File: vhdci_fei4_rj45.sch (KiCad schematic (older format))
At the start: 43 parts, among them J1 71430-015, J2 RJ45, J3 RJ45, J4 RJ45, J5 RJ45, J6 RJ45, J7 RJ45, J8 RJ45, J9 RJ45, P1 USB_OTG, U1 LM317_SOT223

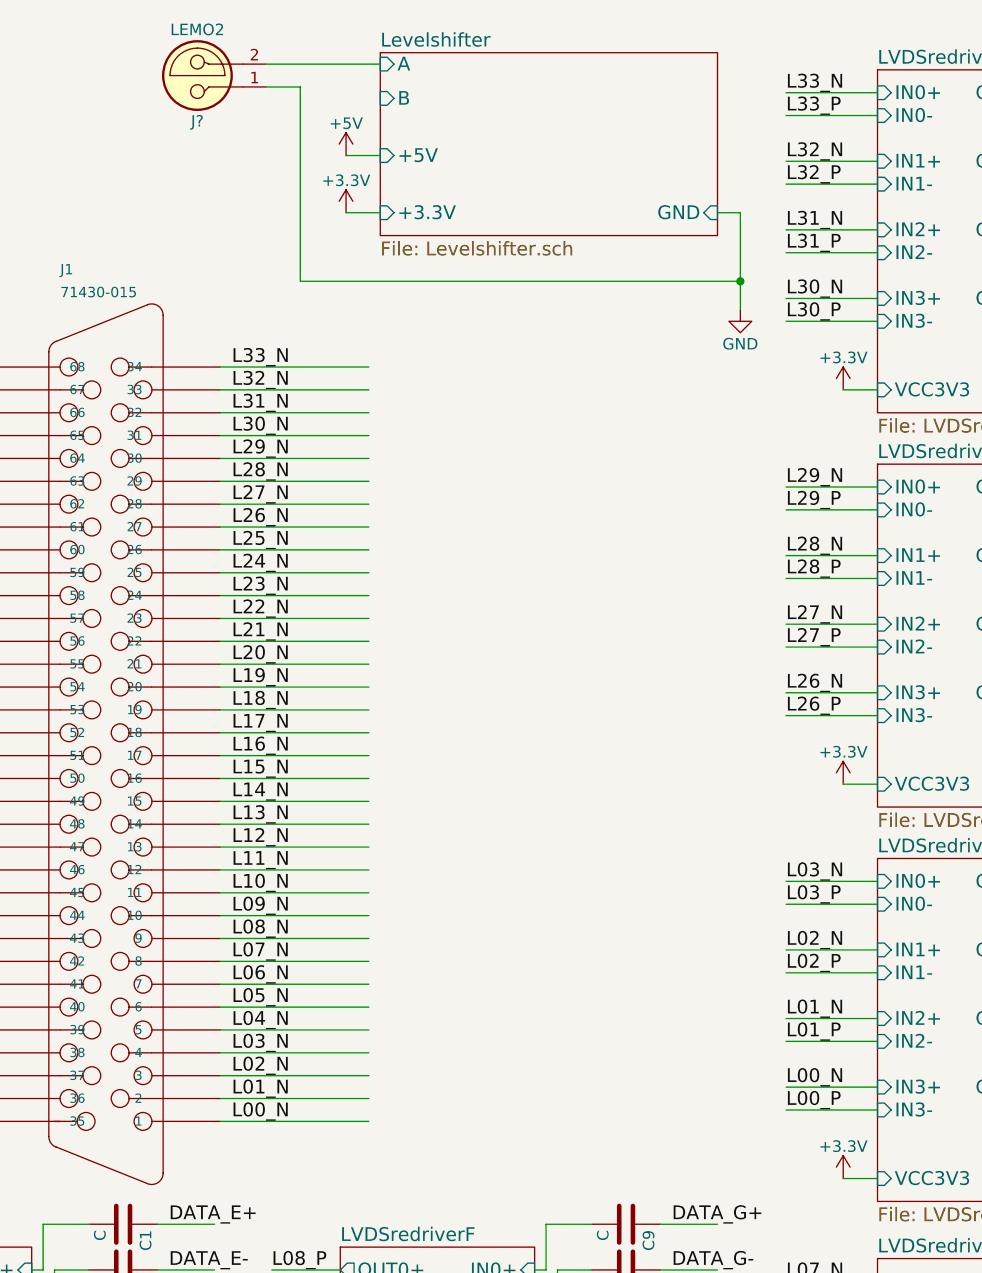
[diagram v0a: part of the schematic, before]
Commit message: Resize Levelshifter sheet. Create 3
Signed-off-by: katie dunne <kedunne@lbl.gov>
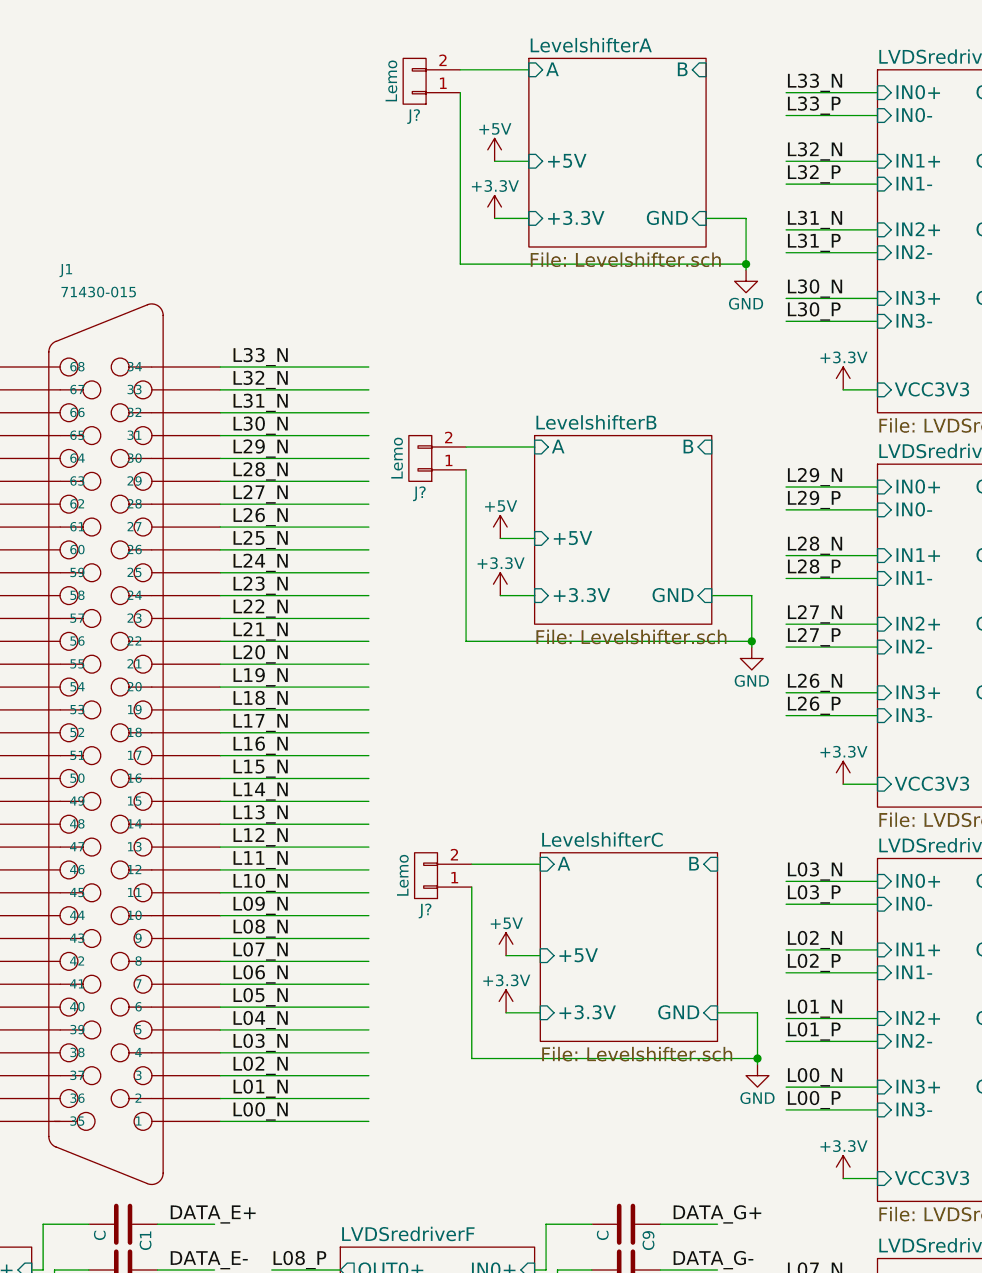
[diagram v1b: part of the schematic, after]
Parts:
- removed J?: LEMO2, symbol LEMO2
- added J? (x3): Lemo, symbol CONN_01X02
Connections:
- wire segments 305 -> 318
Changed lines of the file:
@@
 $Descr A4 11693 8268
 encoding utf-8
-Sheet 1 8
+Sheet 1 10
 Title "VHDCI FE-I4 RJ45 Adapter"
 Date "2017-05-05"
@@
 +5V
 $Sheet
-S 3275 775  1475 800
+S 3925 800  775  825
 U 59133F97
-F0 "Levelshifter" 60
+F0 "LevelshifterA" 60
 F1 "Levelshifter.sch" 60
-F2 "A" I L 3275 825 60
-F3 "+5V" I L 3275 1225 60
-F4 "+3.3V" I L 3275 1475 60
-F5 "B" I L 3275 975 60
-F6 "GND" I R 4750 1475 60
+F2 "A" I L 3925 850 60
+F3 "+5V" I L 3925 1250 60
+F4 "+3.3V" I L 3925 1500 60
+F5 "B" I R 4700 850 60
+F6 "GND" I R 4700 1500 60
 $EndSheet
 $Comp
 L +3.3V #PWR?
 U 1 1 5913F6A0
-P 3125 1475
-F 0 "#PWR?" H 3125 1325 50  0001 C CNN
-F 1 "+3.3V" H 3125 1615 50  0000 C CNN
-F 2 "" H 3125 1475 50  0000 C CNN
-F 3 "" H 3125 1475 50  0000 C CNN
-	1    3125 1475
-	1    0    0    -1
-$EndComp
-Wire Wire Line
-	3125 1475 3275 1475
+P 3775 1500
+F 0 "#PWR?" H 3775 1350 50  0001 C CNN
+F 1 "+3.3V" H 3775 1640 50  0000 C CNN
+F 2 "" H 3775 1500 50  0000 C CNN
+F 3 "" H 3775 1500 50  0000 C CNN
+	1    3775 1500
+	1    0    0    -1
+$EndComp
+Wire Wire Line
+	3775 1500 3925 1500
 $Comp
 L +5V #PWR?
 U 1 1 59140F19
-P 3125 1225
-F 0 "#PWR?" H 3125 1075 50  0001 C CNN
-F 1 "+5V" H 3125 1365 50  0000 C CNN
-F 2 "" H 3125 1225 50  0000 C CNN
-F 3 "" H 3125 1225 50  0000 C CNN
-	1    3125 1225
-	1    0    0    -1
-$EndComp
-Wire Wire Line
-	3125 1225 3275 1225
+P 3775 1250
+F 0 "#PWR?" H 3775 1100 50  0001 C CNN
+F 1 "+5V" H 3775 1390 50  0000 C CNN
+F 2 "" H 3775 1250 50  0000 C CNN
+F 3 "" H 3775 1250 50  0000 C CNN
+	1    3775 1250
+	1    0    0    -1
+$EndComp
+Wire Wire Line
+	3775 1250 3925 1250
 $Comp
 L GND #PWR?
 U 1 1 59143855
-P 4850 1900
-F 0 "#PWR?" H 4850 1650 50  0001 C CNN
-F 1 "GND" H 4850 1750 50  0000 C CNN
-F 2 "" H 4850 1900 50  0001 C CNN
-F 3 "" H 4850 1900 50  0001 C CNN
-	1    4850 1900
-	1    0    0    -1
-$EndComp
-Wire Wire Line
-	4750 1475 4850 1475
-Wire Wire Line
-	4850 1475 4850 1900
-$Comp
-L LEMO2 J?
-U 1 1 59148401
-P 2475 875
-F 0 "J?" H 2475 1075 50  0000 C CNN
-F 1 "LEMO2" H 2475 675 50  0000 C CNN
-F 2 "" H 2475 875 50  0001 C CNN
-F 3 "" H 2475 875 50  0001 C CNN
-	1    2475 875
+P 4875 1725
+F 0 "#PWR?" H 4875 1475 50  0001 C CNN
+F 1 "GND" H 4875 1575 50  0000 C CNN
+F 2 "" H 4875 1725 50  0001 C CNN
+F 3 "" H 4875 1725 50  0001 C CNN
+	1    4875 1725
+	1    0    0    -1
+$EndComp
+Wire Wire Line
+	4700 1500 4875 1500
+$Comp
+L CONN_01X02 J?
+U 1 1 591897DE
+P 3425 900
+F 0 "J?" H 3425 1050 50  0000 C CNN
+F 1 "Lemo" V 3525 900 50  0000 C CNN
+F 2 "" H 3425 900 50  0001 C CNN
+F 3 "" H 3425 900 50  0001 C CNN
+	1    3425 900
 	-1   0    0    1
 $EndComp
-Connection ~ 4850 1775
-Wire Wire Line
-	2775 825  3275 825
-Wire Wire Line
-	2775 925  2925 925
-Wire Wire Line
-	2925 925  2925 1775
-Wire Wire Line
-	2925 1775 4850 1775
+Wire Wire Line
+	4875 1500 4875 1725
+Wire Wire Line
+	3625 1700 4875 1700
+Connection ~ 4875 1700
+$Sheet
+S 3950 2450 775  825
+U 59195600
+F0 "LevelshifterB" 60
+F1 "Levelshifter.sch" 60
+F2 "A" I L 3950 2500 60
+F3 "+5V" I L 3950 2900 60
+F4 "+3.3V" I L 3950 3150 60
+F5 "B" I R 4725 2500 60
+F6 "GND" I R 4725 3150 60
+$EndSheet
+$Comp
+L +3.3V #PWR?
+U 1 1 59195606
+P 3800 3150
+F 0 "#PWR?" H 3800 3000 50  0001 C CNN
+F 1 "+3.3V" H 3800 3290 50  0000 C CNN
+F 2 "" H 3800 3150 50  0000 C CNN
+F 3 "" H 3800 3150 50  0000 C CNN
+	1    3800 3150
+	1    0    0    -1
+$EndComp
+Wire Wire Line
+	3800 3150 3950 3150
+$Comp
+L +5V #PWR?
+U 1 1 5919560D
+P 3800 2900
+F 0 "#PWR?" H 3800 2750 50  0001 C CNN
+F 1 "+5V" H 3800 3040 50  0000 C CNN
+F 2 "" H 3800 2900 50  0000 C CNN
+F 3 "" H 3800 2900 50  0000 C CNN
+	1    3800 2900
+	1    0    0    -1
+$EndComp
+Wire Wire Line
+	3800 2900 3950 2900
+$Comp
+L GND #PWR?
+U 1 1 59195614
+P 4900 3375
+F 0 "#PWR?" H 4900 3125 50  0001 C CNN
+F 1 "GND" H 4900 3225 50  0000 C CNN
+F 2 "" H 4900 3375 50  0001 C CNN
+F 3 "" H 4900 3375 50  0001 C CNN
+	1    4900 3375
+	1    0    0    -1
+$EndComp
+Wire Wire Line
+	4725 3150 4900 3150
+$Comp
+L CONN_01X02 J?
+U 1 1 5919561B
+P 3450 2550
+F 0 "J?" H 3450 2700 50  0000 C CNN
+F 1 "Lemo" V 3550 2550 50  0000 C CNN
+F 2 "" H 3450 2550 50  0001 C CNN
+F 3 "" H 3450 2550 50  0001 C CNN
+	1    3450 2550
+	-1   0    0    1
+$EndComp
+Wire Wire Line
+	4900 3150 4900 3375
+Wire Wire Line
+	3650 3350 4900 3350
+Connection ~ 4900 3350
+$Sheet
+S 3975 4275 775  825
+U 5919615E
+F0 "LevelshifterC" 60
+F1 "Levelshifter.sch" 60
+F2 "A" I L 3975 4325 60
+F3 "+5V" I L 3975 4725 60
+F4 "+3.3V" I L 3975 4975 60
+F5 "B" I R 4750 4325 60
+F6 "GND" I R 4750 4975 60
+$EndSheet
+$Comp
+L +3.3V #PWR?
+U 1 1 59196164
+P 3825 4975
+F 0 "#PWR?" H 3825 4825 50  0001 C CNN
+F 1 "+3.3V" H 3825 5115 50  0000 C CNN
+F 2 "" H 3825 4975 50  0000 C CNN
+F 3 "" H 3825 4975 50  0000 C CNN
+	1    3825 4975
+	1    0    0    -1
+$EndComp
+Wire Wire Line
+	3825 4975 3975 4975
+$Comp
+L +5V #PWR?
+U 1 1 5919616B
+P 3825 4725
+F 0 "#PWR?" H 3825 4575 50  0001 C CNN
+F 1 "+5V" H 3825 4865 50  0000 C CNN
+F 2 "" H 3825 4725 50  0000 C CNN
+F 3 "" H 3825 4725 50  0000 C CNN
+	1    3825 4725
+	1    0    0    -1
+$EndComp
+Wire Wire Line
+	3825 4725 3975 4725
+$Comp
+L GND #PWR?
+U 1 1 59196172
+P 4925 5200
+F 0 "#PWR?" H 4925 4950 50  0001 C CNN
+F 1 "GND" H 4925 5050 50  0000 C CNN
+F 2 "" H 4925 5200 50  0001 C CNN
+F 3 "" H 4925 5200 50  0001 C CNN
+	1    4925 5200
+	1    0    0    -1
+$EndComp
+Wire Wire Line
+	4750 4975 4925 4975
+$Comp
+L CONN_01X02 J?
+U 1 1 59196179
+P 3475 4375
+F 0 "J?" H 3475 4525 50  0000 C CNN
+F 1 "Lemo" V 3575 4375 50  0000 C CNN
+F 2 "" H 3475 4375 50  0001 C CNN
+F 3 "" H 3475 4375 50  0001 C CNN
+	1    3475 4375
+	-1   0    0    1
+$EndComp
+Wire Wire Line
+	4925 4975 4925 5200
+Wire Wire Line
+	3675 5175 4925 5175
+Connection ~ 4925 5175
+Wire Wire Line
+	3625 950  3625 1700
+Wire Wire Line
+	3625 850  3925 850
+Wire Wire Line
+	3650 2600 3650 3350
+Wire Wire Line
+	3650 2500 3950 2500
+Wire Wire Line
+	3675 4325 3975 4325
+Wire Wire Line
+	3675 4425 3675 5175
 $EndSCHEMATC

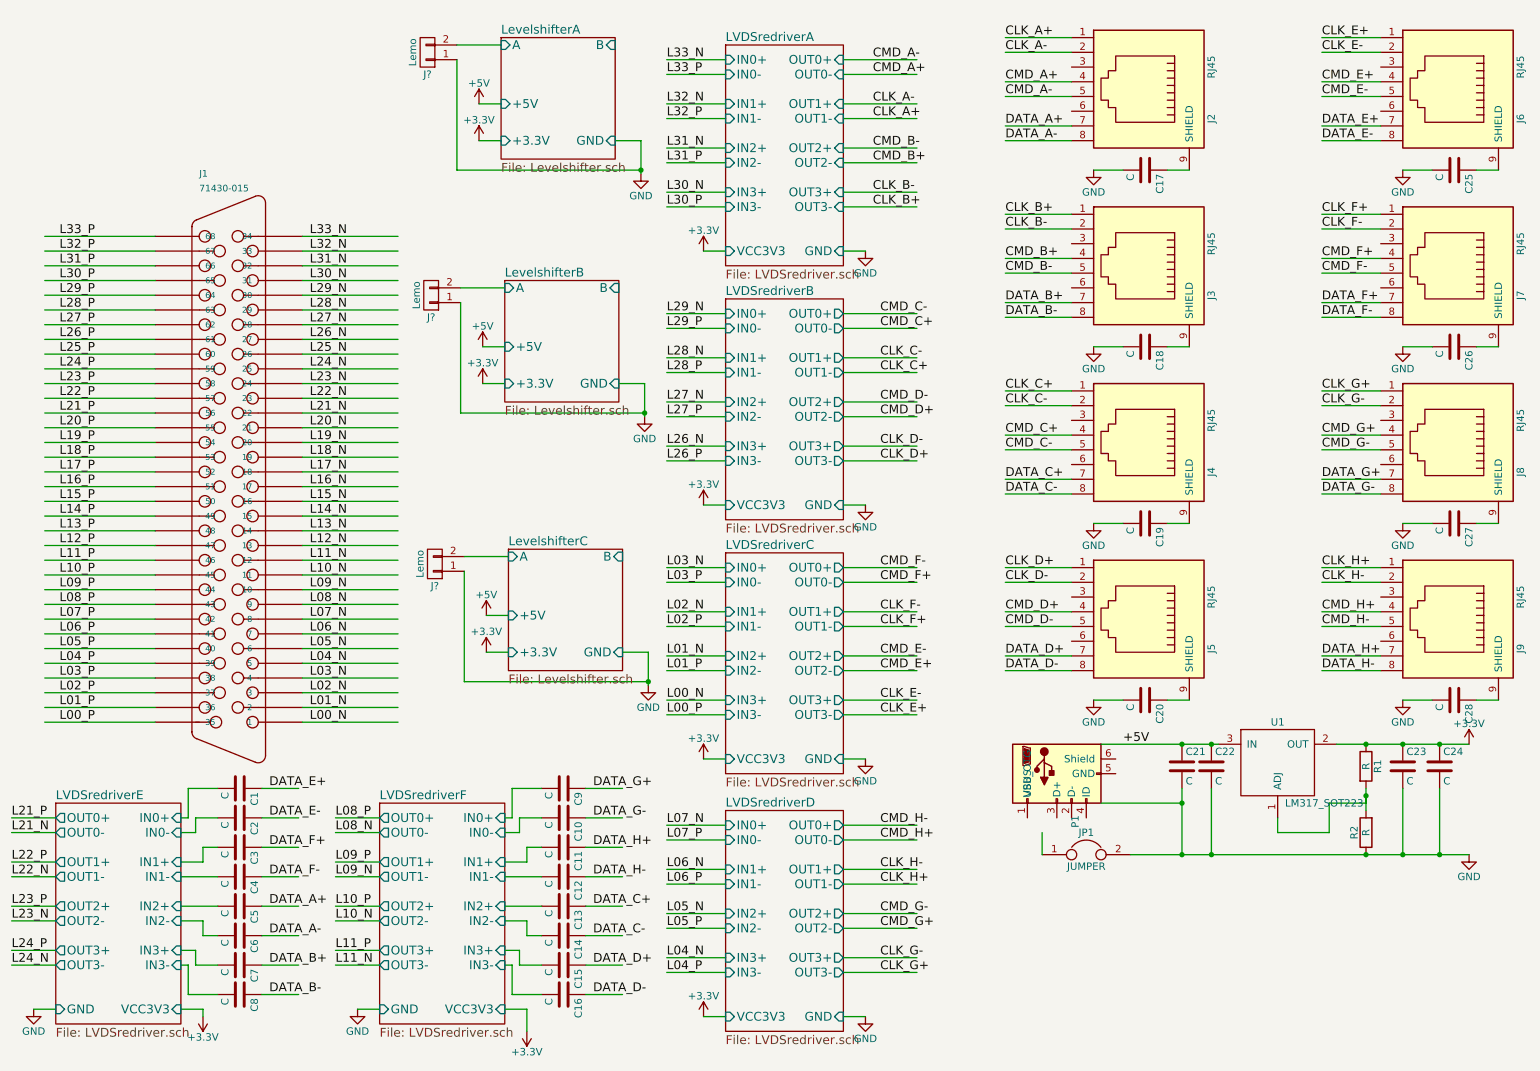
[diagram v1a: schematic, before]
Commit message: Route power, reroute data signals to top layer
Signed-off-by: katie dunne <kedunne@lbl.gov>
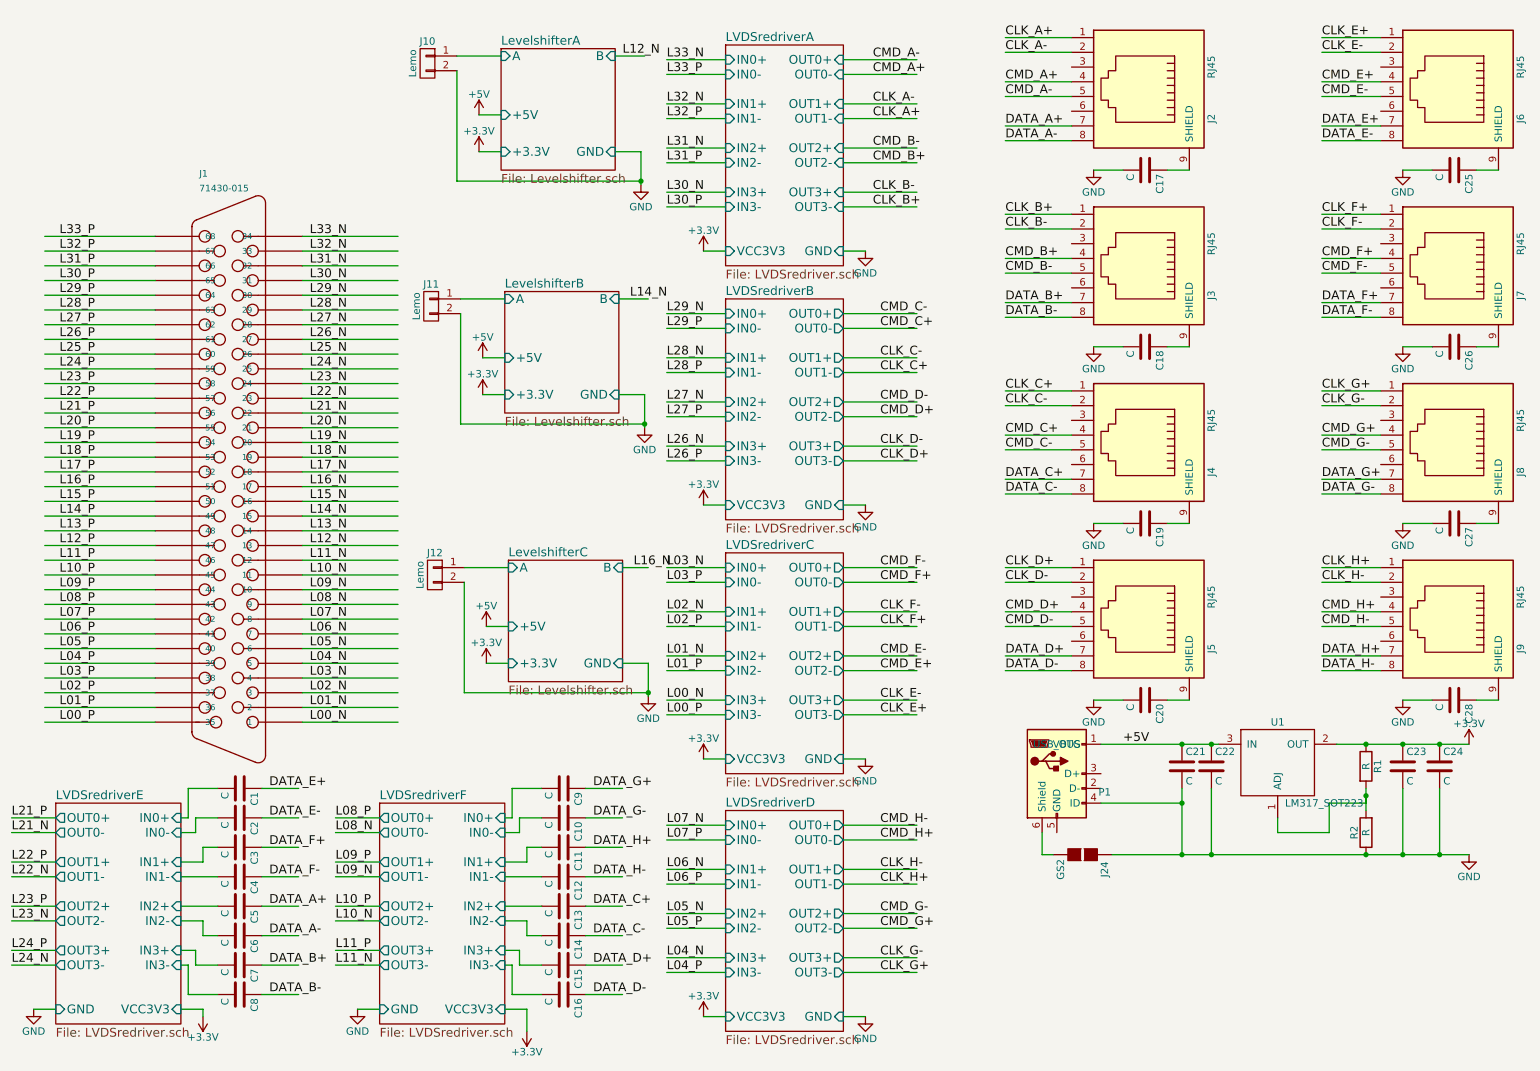
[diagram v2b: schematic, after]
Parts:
- removed JP1: JUMPER, Connectors:GS2, symbol JUMPER
- added J24: GS2, Connectors:GS2, symbol GS2
- J10, J11, J12: renamed from J?; footprint (none) -> w_conn_rf:lemo_epb00250ntn
- U1: footprint TO_SOT_Packages_THT:SOT126_SOT32_Housing_Horizontal -> TO_SOT_Packages_THT:TO-220_Neutral123_Horizontal_LargePads
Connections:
- wire segments 318 -> 322
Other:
- moved on the sheet: J10, J11, J12

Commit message: Route U6, U4, U5
Signed-off-by: Katie Dunne <kdunne@mail.ccsf.edu>
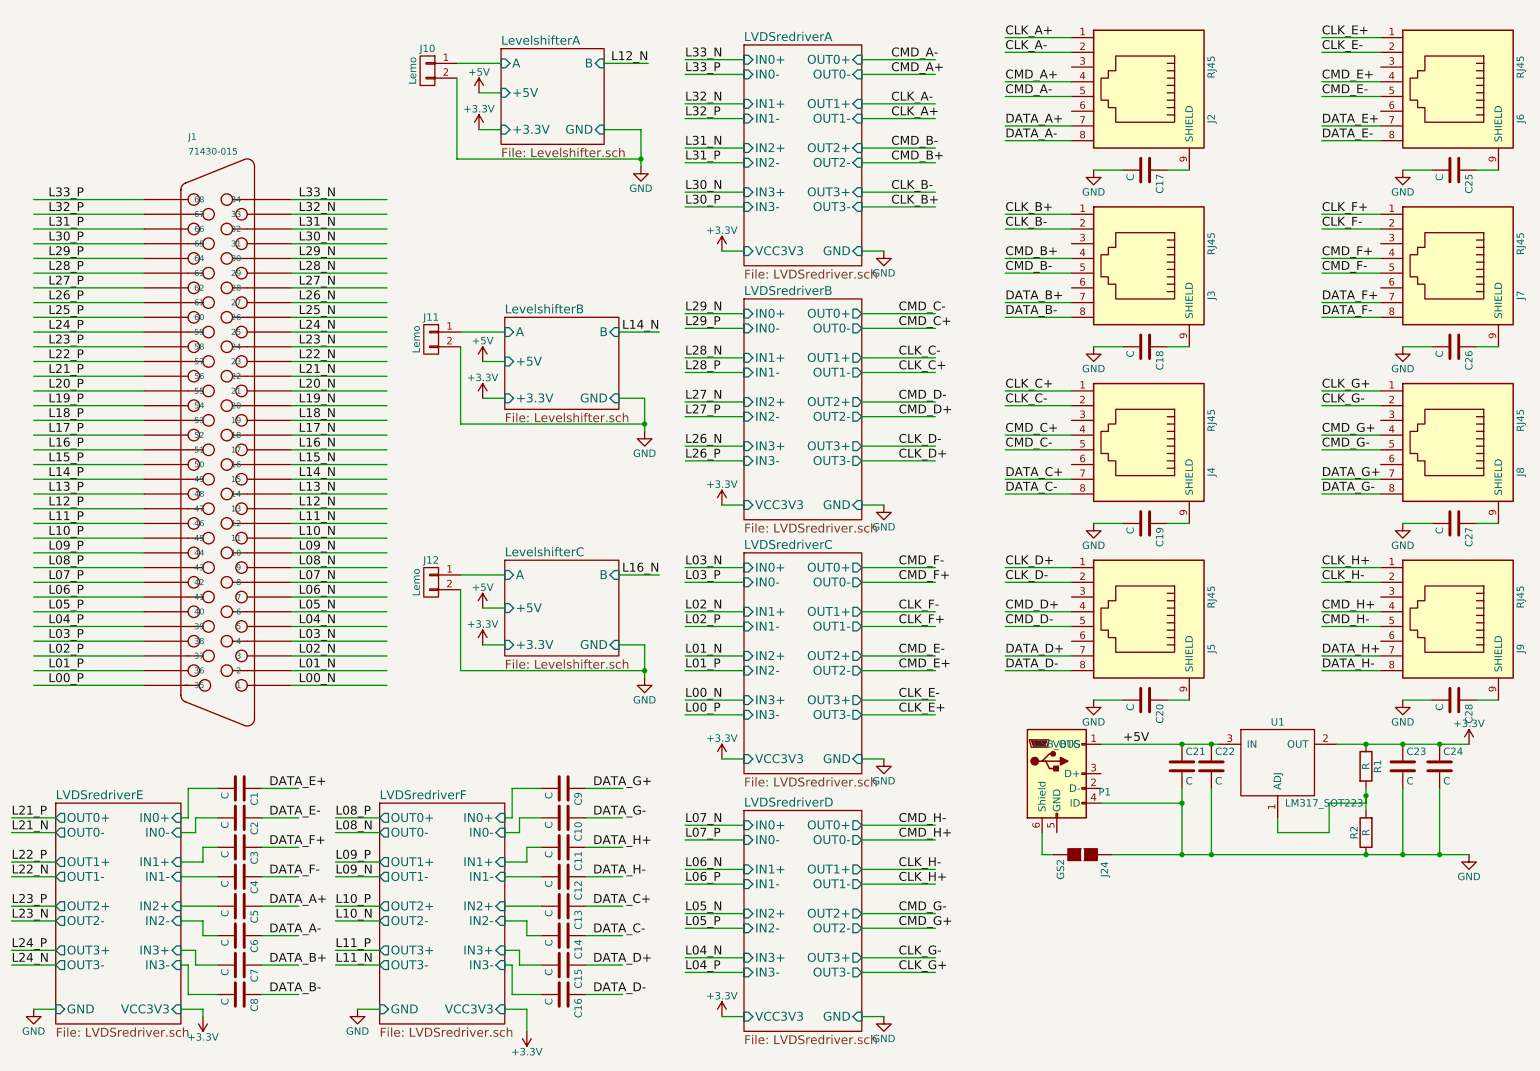
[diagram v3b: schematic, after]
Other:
- moved on the sheet: J1, J10, J11, J12
